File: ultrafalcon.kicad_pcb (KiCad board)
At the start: 2 copper layers, 78 x 78 mm, 49 parts, among them J1 Conn_01x08_Socket, J2 Conn_01x02_Socket, SW1 PER601-P117-N0015, SW2 SW_Push, U1 SK6805-EC15, U10 SK6805-EC15, U11 SK6805-EC15, U12 SK6805-EC15, U13 SK6805-EC15, U14 SK6805-EC15, U15 SK6805-EC15, U16 SK6805-EC15, U17 SK6805-EC15, U18 SK6805-EC15, U19 SK6805-EC15, U2 SK6805-EC15, U20 SK6805-EC15, U21 SK6805-EC15, U22 SK6805-EC15, U23 SK6805-EC15, U24 SK6805-EC15, U25 SK6805-EC15, U26 SK6805-EC15, U27 SK6805-EC15, U28 SK6805-EC15, U29 SK6805-EC15, U3 SK6805-EC15, U30 SK6805-EC15, U4 SK6805-EC15, U5 SK6805-EC15, U6 SK6805-EC15, U7 SK6805-EC15, U8 SK6805-EC15, U9 SK6805-EC15

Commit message: final changes before submitting
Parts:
- removed the LOGO2 at (20.0, 4.61)
- removed the LOGO3 at (9.99, 21.1)
- LOGO2, LOGO3: renamed from G***; value LOGO -> **REF
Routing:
- net GND: track 224.9 -> 227.3 mm
- net Net-(U2-DOUT): track 29.5 -> 30.3 mm
- net VCC: track 482.8 -> 483.3 mm

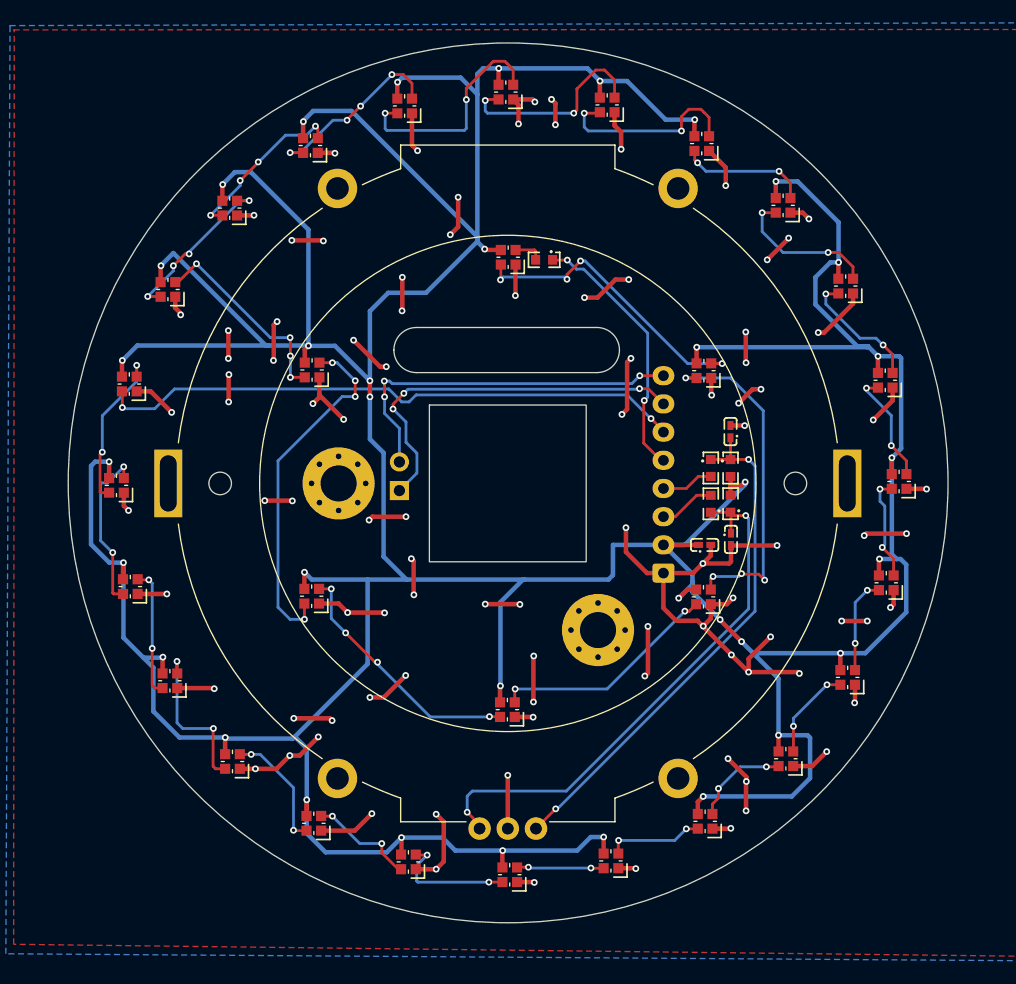
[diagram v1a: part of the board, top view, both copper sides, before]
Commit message: fixed the incorrect footprint silkscreen
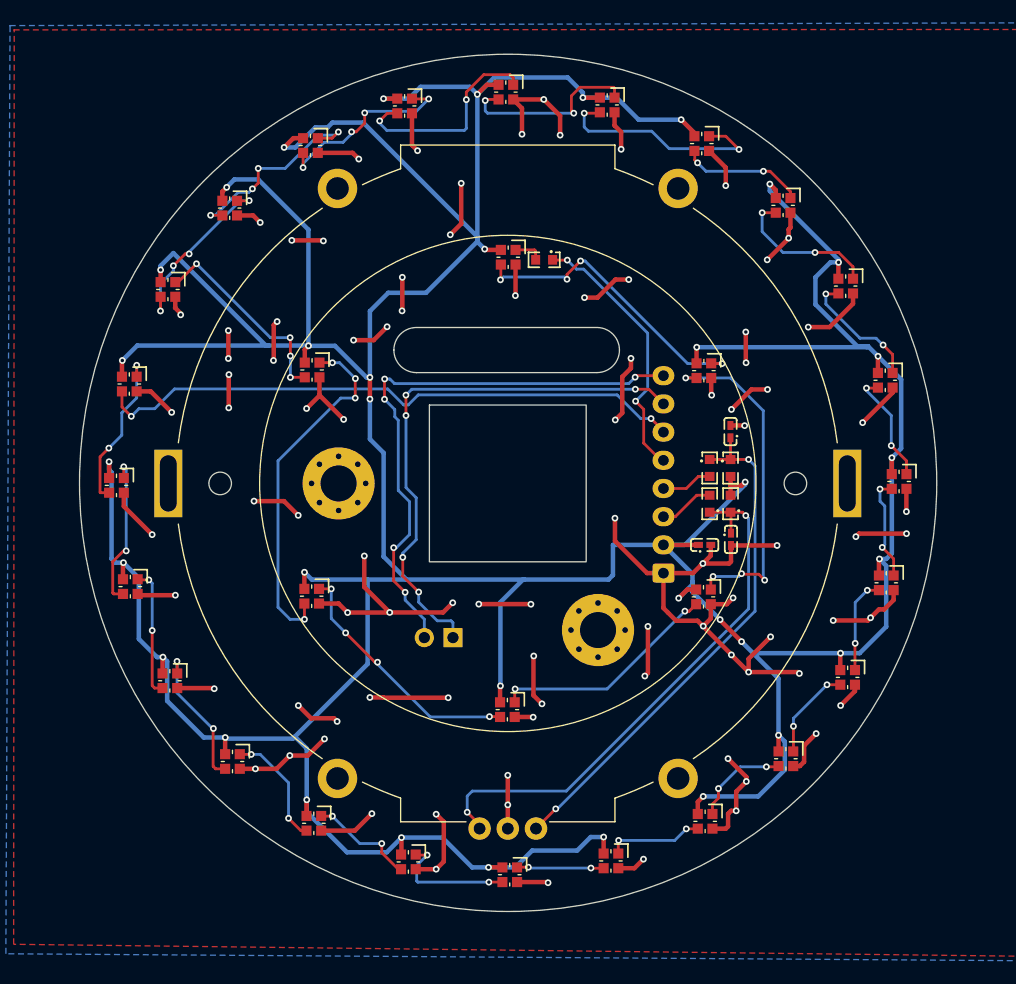
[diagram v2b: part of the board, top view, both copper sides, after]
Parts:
- removed LOGO2: **REF, ct-kicad:pcbway-logo-neg40mm
- moved J2 13.9 mm to (145.1, 113.7), turned to 90 degrees
- moved LOGO3 0.32 mm to (150.3, 72.0)
- moved R4 0.10 mm to (167.9, 101.8)
- moved R5 0.10 mm to (167.9, 98.6)
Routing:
- net GND: track 227.3 -> 268.0 mm, vias 95 -> 90
- net SWITCH_B: track 32.9 -> 50.9 mm, vias 3 -> 5
- net SWITCH_A: track 34.3 -> 48.5 mm, vias 3 -> 5
- net VCC: track 483.3 -> 469.3 mm
- net Net-(U8-DOUT): track 15.1 -> 18.3 mm
- net Net-(U12-DOUT): track 17.4 -> 20.3 mm
- net Net-(U11-DOUT): track 18.3 -> 16.7 mm
- net Net-(U26-DOUT): track 14.5 -> 12.9 mm
- net Net-(U10-DOUT): track 20.1 -> 18.8 mm
- net Net-(U28-DOUT): track 14.8 -> 13.9 mm
- net Net-(U7-DOUT): track 15.1 -> 16.0 mm
- net LED_DO: track 52.4 -> 53.1 mm
- net Net-(U10-DIN): track 16.6 -> 17.3 mm
- net LED_DI: track 23.4 -> 24.0 mm
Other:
- board size 78 x 78 mm -> 76 x 76 mm
- board text added: "v1.1"
- board text removed: "v1.0"
